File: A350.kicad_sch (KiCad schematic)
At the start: 16 parts, among them J1 USB_C_Receptacle_USB2.0_14P, U1 ESP32-S3-WROOM-1, U2 SX1278, U3 PCA9685PW

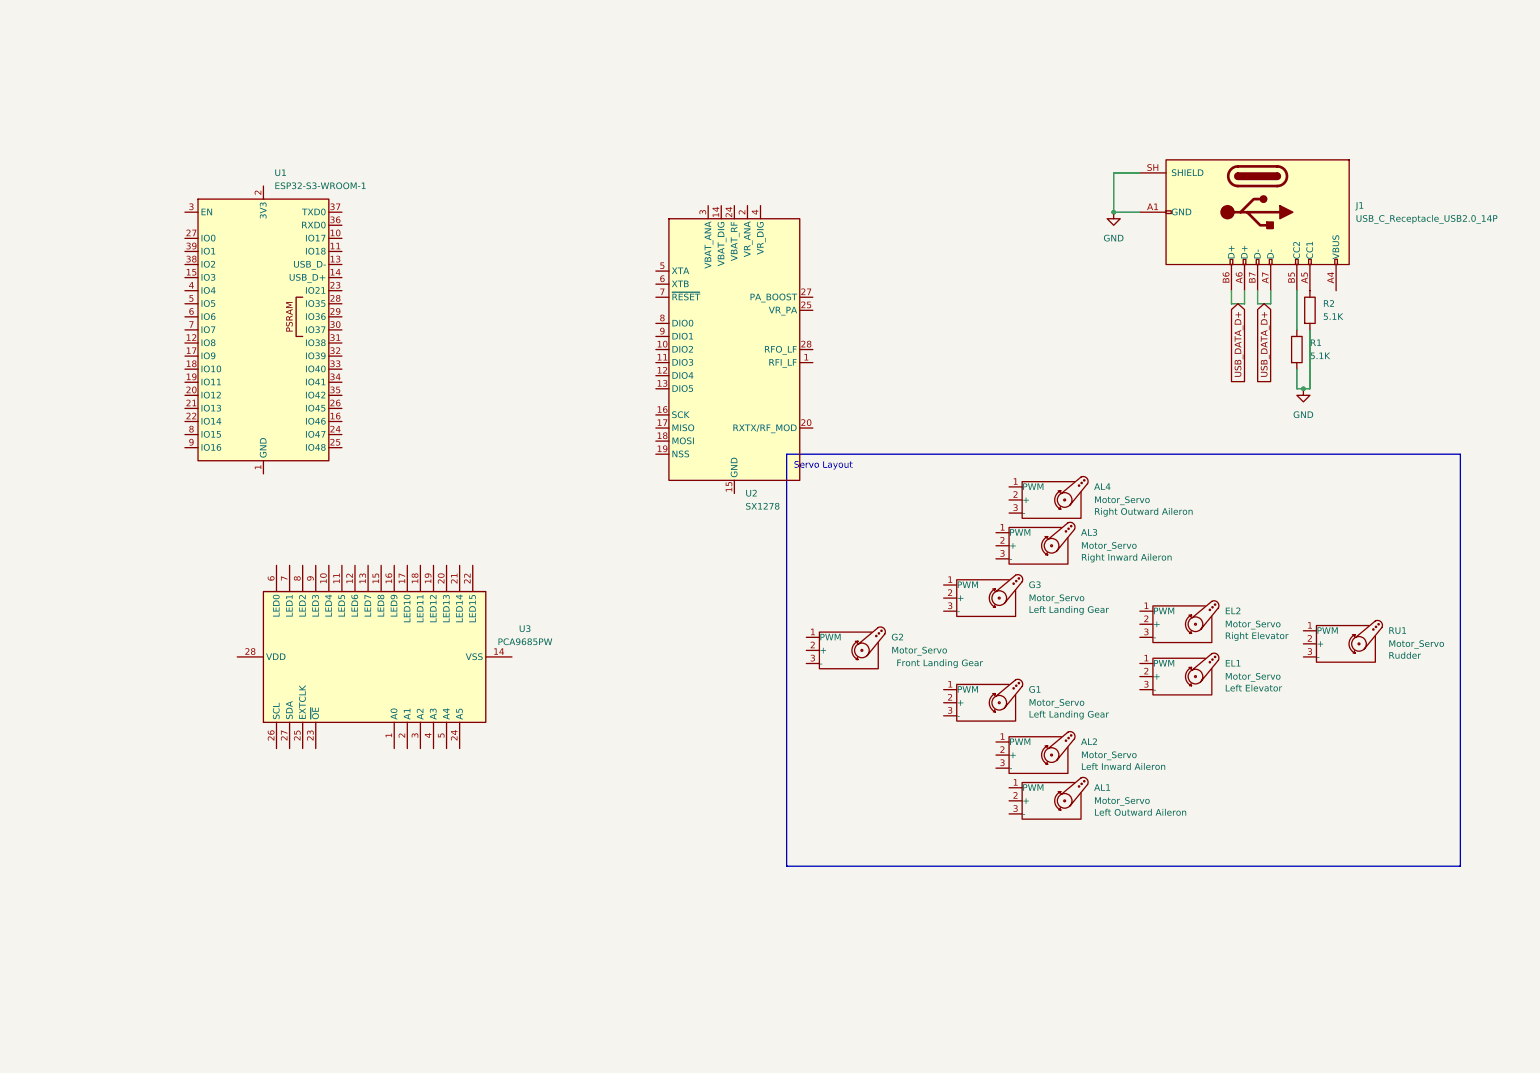
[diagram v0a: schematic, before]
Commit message: added some more parts for schematics, wired some stuff up
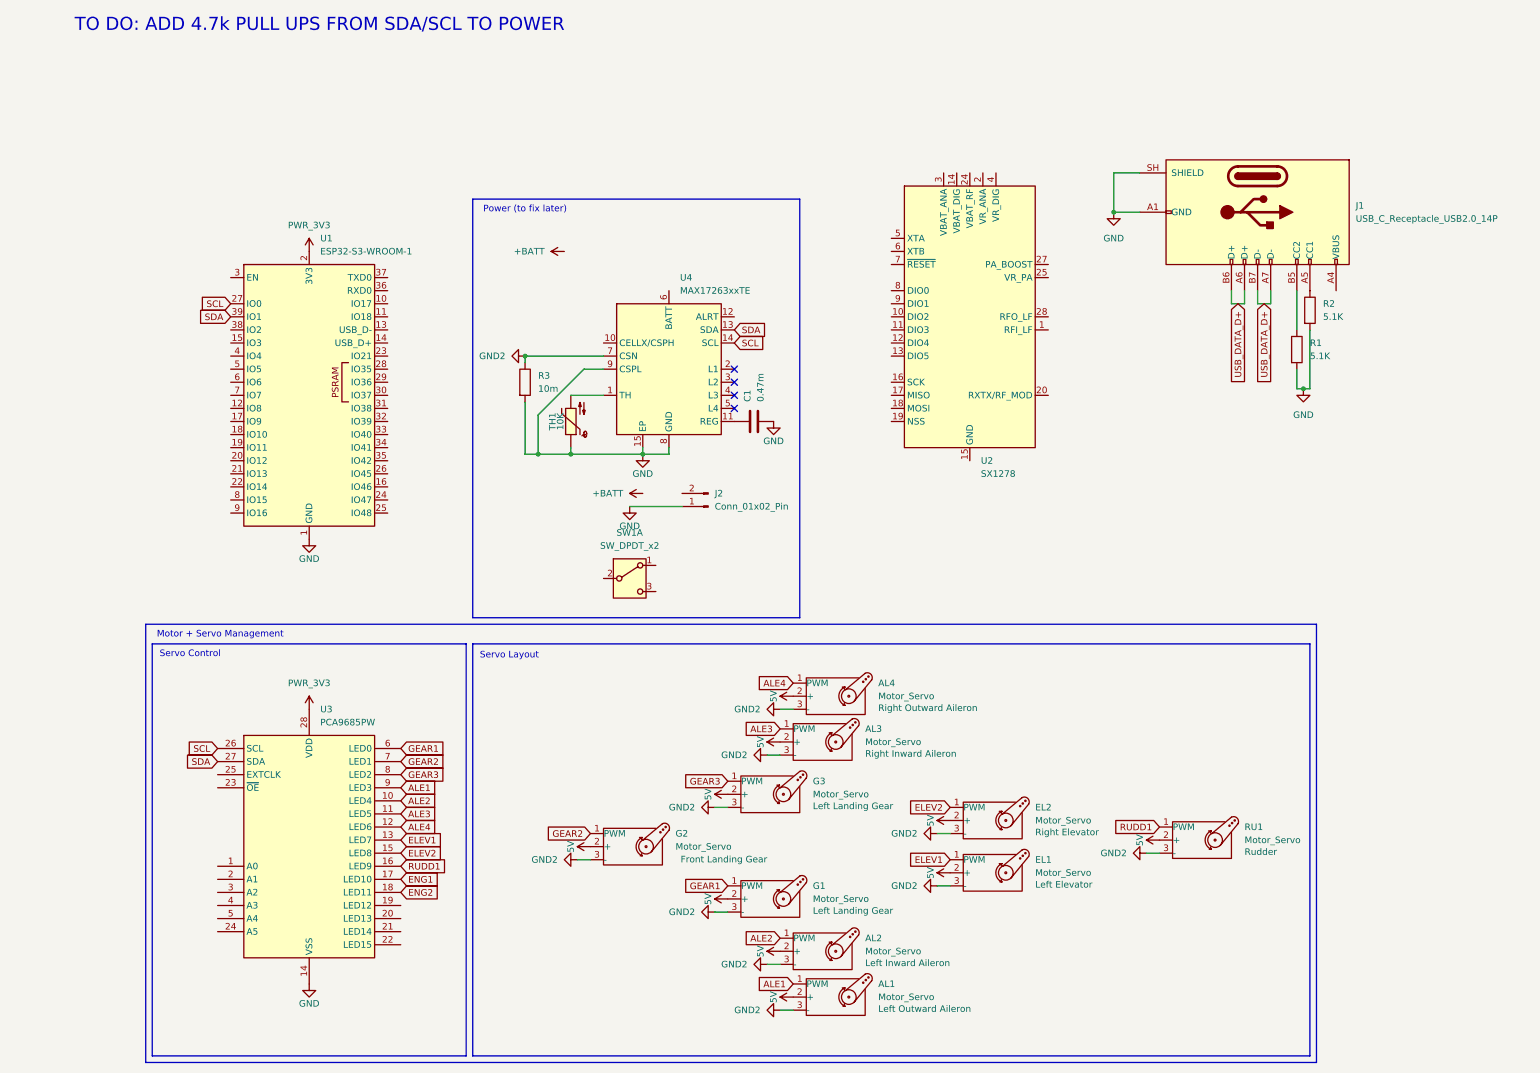
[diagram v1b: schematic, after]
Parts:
- added C1: 0.47m, symbol Device:C
- added J2: Conn_01x02_Pin, Connector_AMASS:AMASS_XT30PW-M_1x02_P2.50mm_Horizontal, symbol Connector:Conn_01x02_Pin
- added R3: 10m, symbol Device:R
- added SW1: SW_DPDT_x2, Button_Switch_THT:SW_PUSH_E-Switch_FS5700DP_DPDT, symbol Switch:SW_DPDT_x2
- added TH1: 10K, PCM_fab:R_1206, symbol PCM_fab:Thermistor_NTC
- added U4: MAX17263xxTE, Package_DFN_QFN:DFN-14-1EP_3x3mm_P0.4mm_EP1.78x2.35mm, symbol Battery_Management:MAX17263xxTE
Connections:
- net GND: now also U1.1 (GND), U1.40 (GND), U1.41 (GND), U3.14 (VSS), C1.1, J2.1 (Pin_1), R3.2, TH1.1, U4.15 (EP), U4.8 (GND), U4.9 (CSPL)
- net GEAR1: now reaches G1.1 (PWM)
- net GEAR1: now also U3.6 (LED0)
- net 5V: now reaches G1.2 (+)
- net 5V: now also AL1.2 (+), AL2.2 (+), AL3.2 (+), AL4.2 (+), EL1.2 (+), EL2.2 (+), G2.2 (+), G3.2 (+), RU1.2 (+)
- net GND2: now reaches G1.3 (-)
- net GND2: now also AL1.3 (-), AL2.3 (-), AL3.3 (-), AL4.3 (-), EL1.3 (-), EL2.3 (-), G2.3 (-), G3.3 (-), RU1.3 (-), R3.1, U4.7 (CSN)
- net ALE2: now reaches AL2.1 (PWM)
- net ALE2: now also U3.10 (LED4)
- net ALE3: now reaches AL3.1 (PWM)
- net ALE3: now also U3.11 (LED5)
- net ELEV1: now reaches EL1.1 (PWM)
- net ELEV1: now also U3.13 (LED7)
- net RUDD1: now reaches RU1.1 (PWM)
- net RUDD1: now also U3.16 (LED9)
- net ELEV2: now reaches EL2.1 (PWM)
- net ELEV2: now also U3.15 (LED8)
- net ALE1: now reaches AL1.1 (PWM)
- net ALE1: now also U3.9 (LED3)
- net GEAR3: now reaches G3.1 (PWM)
- net GEAR3: now also U3.8 (LED2)
- net GEAR2: now reaches G2.1 (PWM)
- net GEAR2: now also U3.7 (LED1)
- net PWR_3V3: now reaches U1.2 (3V3)
- net PWR_3V3: now also U3.28 (VDD)
- net SCL: now reaches U1.27 (IO0)
- net SCL: now also U3.26 (SCL), U4.14 (SCL)
- net SDA: now reaches U1.39 (IO1)
- net SDA: now also U3.27 (SDA), U4.13 (SDA)
- net ALE4: now reaches AL4.1 (PWM)
- net ALE4: now also U3.12 (LED6)
- net ENG1: now reaches U3.17 (LED10)
- net ENG2: now reaches U3.18 (LED11)
- new net: C1.2, U4.11 (REG)
- new net: TH1.2, U4.1 (TH)
- no-connect marks 0 -> 4
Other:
- note added: "Motor + Servo Management"
- note added: "Power (to fix later)"
- note added: "Servo Control"
- note added: "TO DO: ADD 4.7k PULL UPS FROM SDA/SCL TO POWER"
- moved on the sheet: AL1, AL2, AL3, AL4, EL1, EL2, G1, G2, G3, RU1, U1, U2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
